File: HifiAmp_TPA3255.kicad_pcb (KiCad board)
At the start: 4 copper layers, 200 x 150 mm, 124 parts, among them J1 PVDD 48V IN — NEEDS_DATA, J2 RCA L SE, J3 RCA R SE, J301 SPK_L, J302 SPK_R, J4 VOLUME_REMOTE, Q301 IPP330P10NM, Q302 IXTK200N10L2, U1 LM5010ASD, U2 LM2940IMP-12/NOPB, U3 TLV1117-33IDCY, U4 OPA1612AIDR, U5 OPA1612AIDR, U6 TPA3255B, U7 TPS3802K33DCKR, U8 LM5069-2

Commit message: feat(f1.1): route the auxiliary rails, and prove VBG cannot cross
AVDD, DVDD and +12V now reach their decoupling capacitors: 15 segments on
F.Cu, no via, 0.30 mm wide. The class width of 0.8 mm was never an option at
U6's 0.635 mm pitch — 0.30 mm leaves 0.285 mm of clearance where 0.25 is
required, and the classes had to be read from .kicad_pro, not the .kicad_dru.

A first attempt shorted six items: C106, C107, C206 and C207 sit in the
corridor and were missing from the obstacle list. The DRC caught what the
script did not. Those 14 segments were pulled and the geometry recomputed.

VBG stays unrouted, and not for lack of trying. At U6 pin 22 comes before
VBG; at the capacitors C303 comes before C304. The order inverts between
source and target, so any single-layer path crosses — the external detour
runs into AVDD, the local bypass needs 0.75 mm where a 0805 offers 0.65, and
yielding priority hits the same neck. No via was placed: that call is the
user's.

DRC unchanged at 112 silkscreen violations, no clearance, no shorting items,
no dangling track; parity still 3; unconnected 244 to 239, exactly the five
ratsnests predicted.

Co-Authored-By: Claude Opus 5 <noreply@anthropic.com>
Claude-Session: https://claude.ai/code/session_01Q198zQg99VJYE128nree8X
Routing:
- net /DVDD: track 0.00 -> 38.3 mm
- net /AVDD: track 0.00 -> 32.4 mm
- net /+12V: track 0.00 -> 17.3 mm
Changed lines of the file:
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@@
 		(tags "capacitor")
 		(property "Reference" "C310"
-			(at 0 -2.3 -90)
+			(at 0 -2.3 270)
 			(layer "F.SilkS")
 			(effects
@@
 		)
 		(property "Value" "1uF/100V"
-			(at 0 2.3 -90)
+			(at 0 2.3 270)
 			(layer "F.Fab")
 			(effects
@@
 		)
 		(property "Datasheet" ""
-			(at 0 0 -90)
+			(at 0 0 270)
 			(layer "F.Fab")
 			(hide yes)
@@
 		)
 		(property "Description" ""
-			(at 0 0 -90)
+			(at 0 0 270)
 			(layer "F.Fab")
 			(hide yes)
@@
 		)
 		(property "KiLib_Generator" "SMD_2terminal_chip_molded"
-			(at 0 0 -90)
+			(at 0 0 270)
 			(layer "F.SilkS")
 			(hide yes)
@@
 		)
 		(fp_text user "${REFERENCE}"
-			(at 0 0 -90)
+			(at 0 0 270)
 			(layer "F.Fab")
 			(effects
@@
 	)
 	(segment
+		(start 288.7125 181.6675)
+		(end 288.7125 185.5)
+		(width 0.3)
+		(layer "F.Cu")
+		(net "/+12V")
+	)
+	(segment
+		(start 292.225 165)
+		(end 292.225 166)
+		(width 0.3)
+		(layer "F.Cu")
+		(net "/+12V")
+	)
+	(segment
+		(start 292.225 185.5)
+		(end 292.225 184)
+		(width 0.3)
+		(layer "F.Cu")
+		(net "/+12V")
+	)
+	(segment
+		(start 288.7125 168.3325)
+		(end 288.7125 165)
+		(width 0.3)
+		(layer "F.Cu")
+		(net "/+12V")
+	)
+	(segment
+		(start 288.7125 165)
+		(end 292.225 165)
+		(width 0.3)
+		(layer "F.Cu")
+		(net "/+12V")
+	)
+	(segment
+		(start 288.7125 185.5)
+		(end 292.225 185.5)
+		(width 0.3)
+		(layer "F.Cu")
+		(net "/+12V")
+	)
+	(segment
+		(start 288.7125 181.0325)
+		(end 288.7125 181.6675)
+		(width 0.3)
+		(layer "F.Cu")
+		(net "/+12V")
+	)
+	(segment
 		(start 279.9 177.2225)
 		(end 281.2875 177.2225)
@@
 	)
 	(segment
+		(start 298.7 195)
+		(end 292.05 195)
+		(width 0.3)
+		(layer "F.Cu")
+		(net "/DVDD")
+	)
+	(segment
+		(start 288.7125 175.3175)
+		(end 298.7 175.3175)
+		(width 0.3)
+		(layer "F.Cu")
+		(net "/DVDD")
+	)
+	(segment
+		(start 298.7 175.3175)
+		(end 298.7 195)
+		(width 0.3)
+		(layer "F.Cu")
+		(net "/DVDD")
+	)
+	(segment
+		(start 292.05 195)
+		(end 292.05 193)
+		(width 0.3)
+		(layer "F.Cu")
+		(net "/DVDD")
+	)
+	(segment
+		(start 298.7 158.8)
+		(end 292.05 158.8)
+		(width 0.3)
+		(layer "F.Cu")
+		(net "/AVDD")
+	)
+	(segment
+		(start 292.05 158.8)
+		(end 292.05 160)
+		(width 0.3)
+		(layer "F.Cu")
+		(net "/AVDD")
+	)
+	(segment
+		(start 288.7125 173.4125)
+		(end 298.7 173.4125)
+		(width 0.3)
+		(layer "F.Cu")
+		(net "/AVDD")
+	)
+	(segment
+		(start 298.7 173.4125)
+		(end 298.7 158.8)
+		(width 0.3)
+		(layer "F.Cu")
+		(net "/AVDD")
+	)
+	(segment

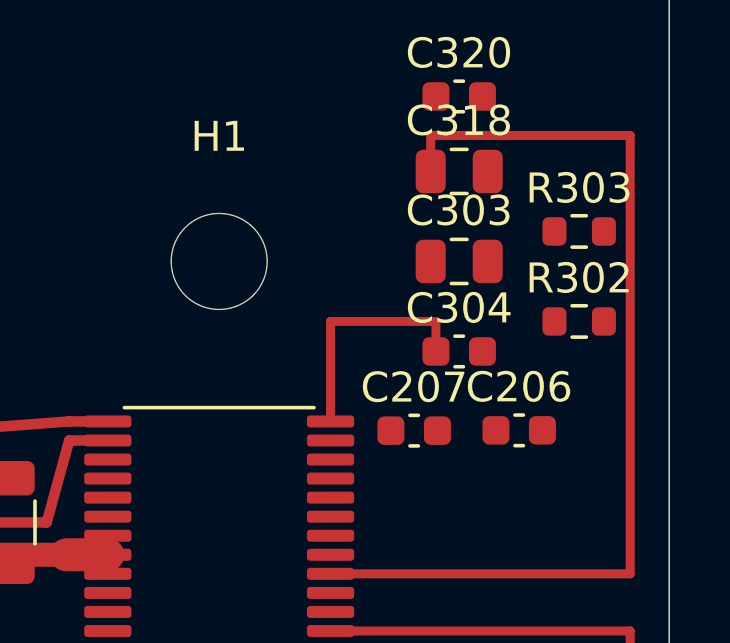
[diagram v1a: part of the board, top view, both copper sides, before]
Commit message: feat(f1.1): swap C303 and C304 so VBG no longer has to cross
The crossing came from the order of the endpoints inverting between U6 and
the capacitor row, so the endpoints are what moved: C303 takes y=166 and
C304 takes y=163. The order now matches on both sides and VBG reaches its
capacitor in a straight run — 4 segments, 14.0 mm at 0.25 mm — with +12V
pin 22 following in 3 segments. Still no via anywhere on the board.

Moving an 0805 into an 0603 row is fine here: both sit at 0 degrees, so the
long axis runs in x and the row only grows 0.5 mm in y. The real obstacle
was never the neighbouring part but the GND pads of C207 and C303, which a
first route came within -0.125 mm of. The clearance check caught it before
the DRC did.

The IPC move left three obsolete /+12V segments dangling behind it. Query a
net's traces after moving one of its components.

Unconnected 239 to 238, parity still 3, no clearance, shorting or dangling
items, 124 footprints with exactly two (at) lines swapped. Silkscreen went
112 to 113 as C303 now overlaps the reference fields of C206 and C207 —
cosmetic, and it joins the pile to be cleared in one pass.

F1.1 is closed.

Co-Authored-By: Claude Opus 5 <noreply@anthropic.com>
Claude-Session: https://claude.ai/code/session_01Q198zQg99VJYE128nree8X
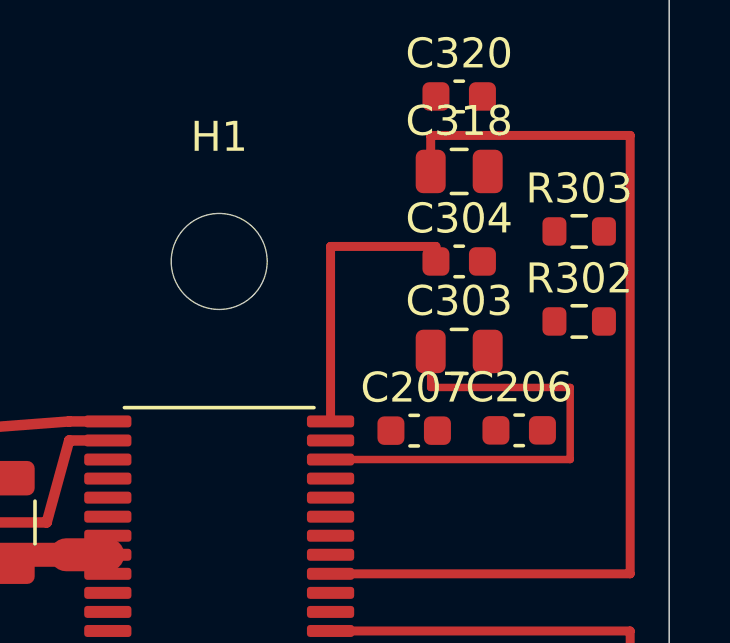
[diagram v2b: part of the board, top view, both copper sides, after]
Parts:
- moved C303 3.00 mm to (293.0, 166.0)
- moved C304 3.00 mm to (293.0, 163.0)
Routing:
- net /VBG: track 0.00 -> 16.2 mm
- net /+12V: track 17.3 -> 19.3 mm
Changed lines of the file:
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@@
 	(footprint "Capacitor_SMD:C_0805_2012Metric"
 		(layer "F.Cu")
-		(at 293 163)
+		(at 293 166)
 		(descr "Capacitor SMD 0805 (2012 Metric), square (rectangular) end terminal, IPC-7351 nominal, (Body size source: IPC-SM-782 page 76, https://www.pcb-3d.com/wordpress/wp-content/uploads/ipc-sm-782a_amendment_1_and_2.pdf, https://docs.google.com/spreadsheets/d/1BsfQQcO9C6DZCsRaXUlFlo91Tg2WpOkGARC1WS5S8t0/edit?usp=sharing)")
 		(tags "capacitor")
@@
 		(sheetname "/")
 		(sheetfile "HifiAmp_TPA3255.kicad_sch")
-		(units
-			(unit
-				(name "A")
-				(pins "1" "2")
-			)
-		)
 		(attr smd)
 		(duplicate_pad_numbers_are_jumpers no)
@@
 	(footprint "Capacitor_SMD:C_0603_1608Metric"
 		(layer "F.Cu")
-		(at 293 166)
+		(at 293 163)
 		(descr "Capacitor SMD 0603 (1608 Metric), square (rectangular) end terminal, IPC-7351 nominal, (Body size source: IPC-SM-782 page 76, https://www.pcb-3d.com/wordpress/wp-content/uploads/ipc-sm-782a_amendment_1_and_2.pdf)")
 		(tags "capacitor")
@@
 		(sheetname "/")
 		(sheetfile "HifiAmp_TPA3255.kicad_sch")
-		(units
-			(unit
-				(name "A")
-				(pins "1" "2")
-			)
-		)
 		(attr smd)
 		(duplicate_pad_numbers_are_jumpers no)
@@
 	)
 	(segment
-		(start 292.225 165)
-		(end 292.225 166)
+		(start 288.7125 168.3325)
+		(end 288.7125 162.5)
 		(width 0.3)
 		(layer "F.Cu")
@@
 	)
 	(segment
-		(start 292.225 185.5)
-		(end 292.225 184)
+		(start 292.225 162.5)
+		(end 292.225 163)
 		(width 0.3)
 		(layer "F.Cu")
@@
 	)
 	(segment
-		(start 288.7125 168.3325)
-		(end 288.7125 165)
+		(start 292.225 185.5)
+		(end 292.225 184)
 		(width 0.3)
 		(layer "F.Cu")
@@
 	)
 	(segment
-		(start 288.7125 165)
-		(end 292.225 165)
+		(start 288.7125 162.5)
+		(end 292.225 162.5)
 		(width 0.3)
 		(layer "F.Cu")
@@
 	)
 	(segment
+		(start 288.7125 169.6025)
+		(end 296.7 169.6025)
+		(width 0.25)
+		(layer "F.Cu")
+		(net "/VBG")
+	)
+	(segment
+		(start 292.05 167.2)
+		(end 292.05 166)
+		(width 0.25)
+		(layer "F.Cu")
+		(net "/VBG")
+	)
+	(segment
+		(start 296.7 167.2)
+		(end 292.05 167.2)
+		(width 0.25)
+		(layer "F.Cu")
+		(net "/VBG")
+	)
+	(segment
+		(start 296.7 169.6025)
+		(end 296.7 167.2)
+		(width 0.25)
+		(layer "F.Cu")
+		(net "/VBG")
+	)
+	(segment

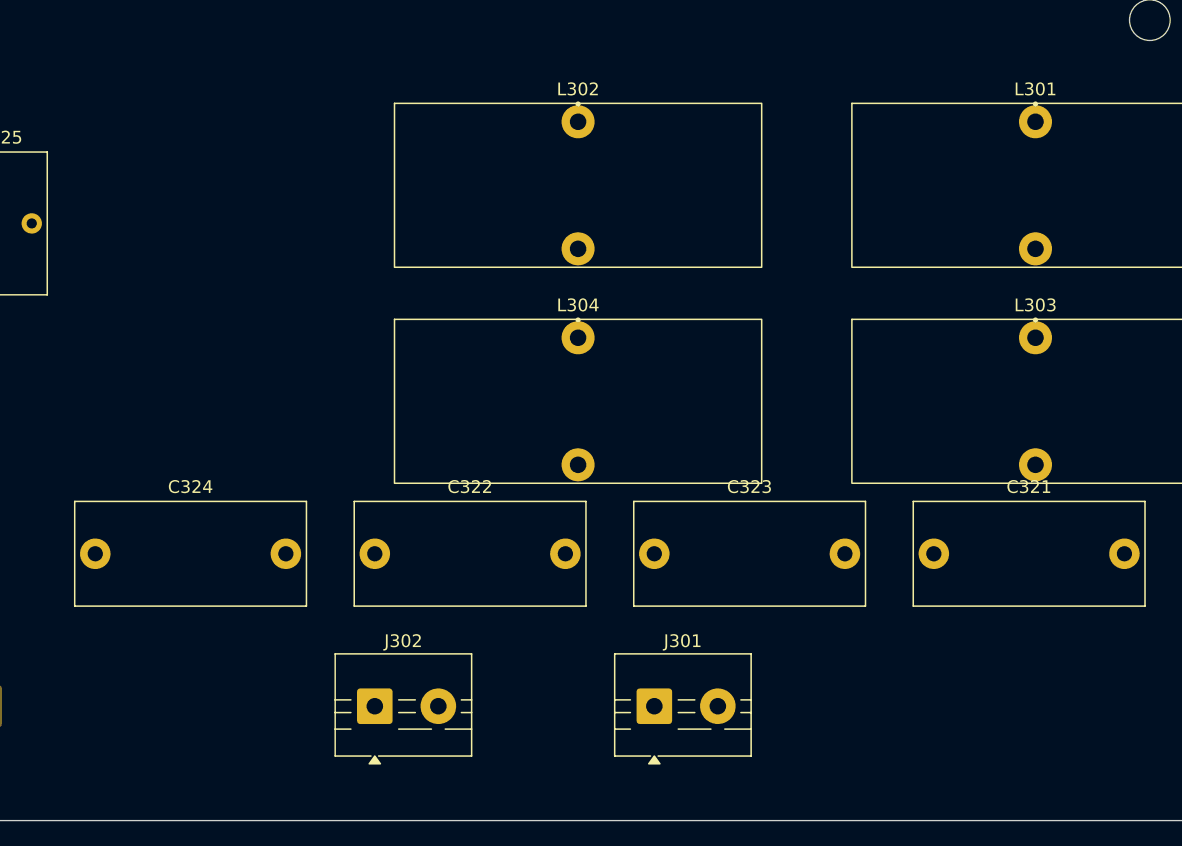
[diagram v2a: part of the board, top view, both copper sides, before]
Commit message: feat(f1.2-a): untangle the outputs, then route them at their class width
The four filtered outputs could not be routed on F.Cu at all with the E1.5
placement, and the obstacle was an order, not a width. At the filter caps the
x-order was D, B, C, A; at the terminals, fixed by BTL pairing, it is D, C, B,
A. B and C transposed force a crossing on any single-layer path, detours along
the board edge included, since D must itself sweep the band to reach its cap at
x = 202. This is exactly the interleaving E1.5 measured and handed to F1.

The fix moves nothing new: L302 and L303 swap slots, C322 and C323 swap slots,
identical parts into identical positions, rotations untouched. The cap order
becomes D, C, B, A and the topology turns planar. It also groups each bridge
pair into one column -- A and B at x = 276, C and D at x = 240 -- which is what
the F1 pairing constraint asked for and the placement could not give. Every
L-to-R symmetry vector stays exact and the intra-pair ones become exact too.

The 0.5 mm draft this replaces carried 1.45 A at IPC-2221, 35 um, dT = 10 C,
for 5 A to pass. At 3.00 mm the track carries 5.3 A, and the class width proves
tenable here: outside a fine-pitch package the obstacles are spaced through-hole
pads. Tightest corridors, checked by hand then by DRC: 0.70 mm under L302's pad,
0.75 mm above the filter caps, 1.50 mm to the board edge.

Pairing target set on real track lengths and met without meanders: 12.0 mm
within A/B, 10.0 mm within C/D, against 8.5 and 26.4 mm as placed. 12 mm of
3 mm track is 2 mOhm and 10 nH against 15 uH and 31 mOhm of series inductor --
meandering would cost copper and loop area for nothing measurable.

DRC 113 violations, the same silkscreen ones as the baseline; no clearance, no
shorting_items, no track_dangling, no solder_mask_bridge, no edge clearance.
Unconnected 238 to 230, the eight predicted ratsnests. Parity still 3. Checked
independently: 58 segments all on F.Cu, 0 vias, zero intersection between the
23 ne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
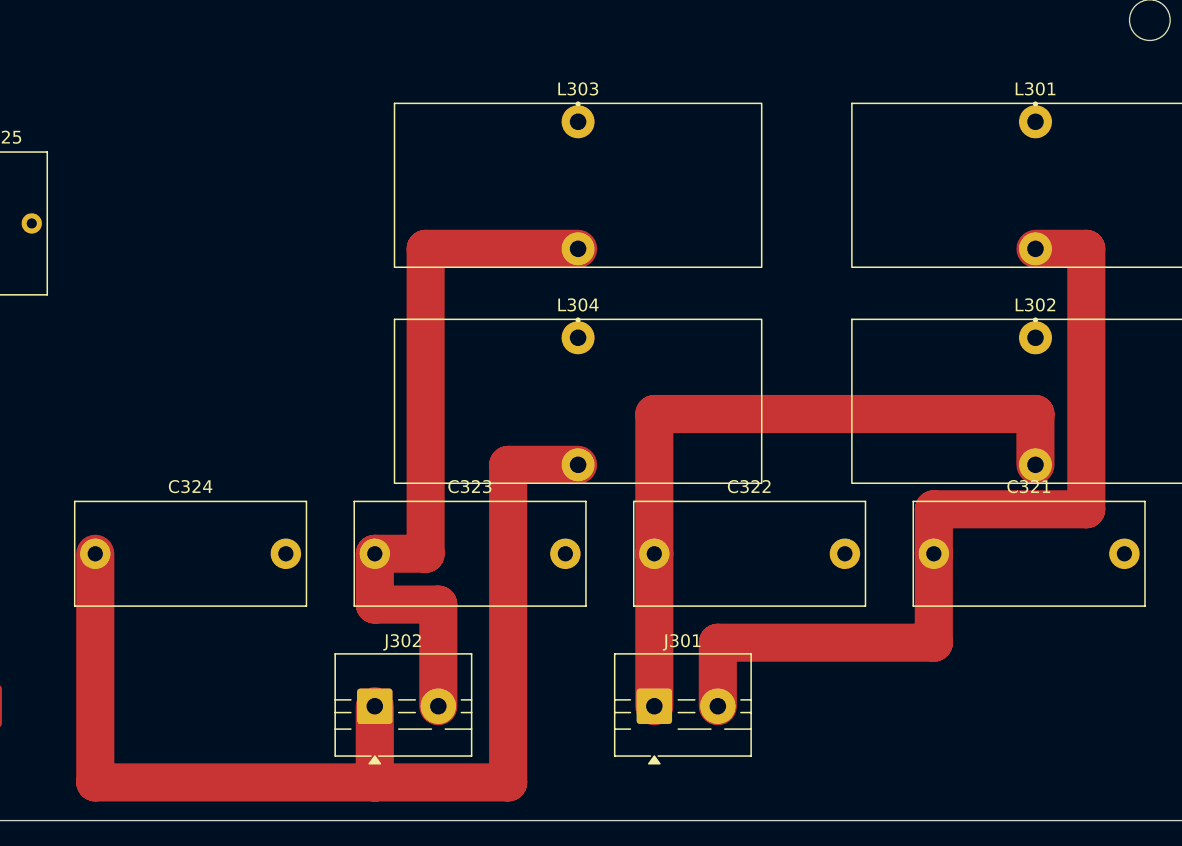
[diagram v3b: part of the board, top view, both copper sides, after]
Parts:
- moved L302 39.8 mm to (276.0, 212.0)
- moved L303 39.8 mm to (240.0, 195.0)
- moved C322 22.0 mm to (246.0, 229.0)
- moved C323 22.0 mm to (224.0, 229.0)
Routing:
- net /OUT_D_F: track 0.00 -> 87.0 mm
- net /OUT_A_F: track 0.00 -> 69.0 mm
- net /OUT_C_F: track 0.00 -> 57.0 mm
- net /OUT_B_F: track 0.00 -> 57.0 mm
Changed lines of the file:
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@@
 	(footprint "Capacitor_THT:C_Rect_L18.0mm_W8.0mm_P15.00mm_FKS3_FKP3"
 		(layer "F.Cu")
-		(at 224 229)
+		(at 246 229)
 		(descr "C, Rect series, Radial, pin pitch=15.00mm, length*width=18*8mm^2, Capacitor, http://www.wima.com/EN/WIMA_FKS_3.pdf")
 		(tags "C Rect series Radial pin pitch 15.00mm length 18mm width 8mm Capacitor")
@@
 	(footprint "Capacitor_THT:C_Rect_L18.0mm_W8.0mm_P15.00mm_FKS3_FKP3"
 		(layer "F.Cu")
-		(at 246 229)
+		(at 224 229)
 		(descr "C, Rect series, Radial, pin pitch=15.00mm, length*width=18*8mm^2, Capacitor, http://www.wima.com/EN/WIMA_FKS_3.pdf")
 		(tags "C Rect series Radial pin pitch 15.00mm length 18mm width 8mm Capacitor")
@@
 	(footprint "HifiAmp_TPA3255_Local:L_Toroid_Vertical_L28.6mm_W12.3mm_P10.00mm_Coilcraft_PA6331"
 		(layer "F.Cu")
-		(at 240 195)
+		(at 276 212)
 		(descr "Coilcraft PA6331-AE, toroidal power inductor 15uH, vertical mount, iron powder core, THT, body 28.6mm max dia x 12.3mm max thickness, pin pitch 10.0+/-0.5mm")
 		(property "Reference" "L302"
@@
 	(footprint "HifiAmp_TPA3255_Local:L_Toroid_Vertical_L28.6mm_W12.3mm_P10.00mm_Coilcraft_PA6331"
 		(layer "F.Cu")
-		(at 276 212)
+		(at 240 195)
 		(descr "Coilcraft PA6331-AE, toroidal power inductor 15uH, vertical mount, iron powder core, THT, body 28.6mm max dia x 12.3mm max thickness, pin pitch 10.0+/-0.5mm")
 		(property "Reference" "L303"
@@
 	)
 	(segment
+		(start 234.5 222)
+		(end 234.5 247)
+		(width 3)
+		(layer "F.Cu")
+		(net "/OUT_D_F")
+	)
+	(segment
+		(start 202 247)
+		(end 202 229)
+		(width 3)
+		(layer "F.Cu")
+		(net "/OUT_D_F")
+	)
+	(segment
+		(start 234.5 247)
+		(end 224 247)
+		(width 3)
+		(layer "F.Cu")
+		(net "/OUT_D_F")
+	)
+	(segment
+		(start 240 222)
+		(end 234.5 222)
+		(width 3)
+		(layer "F.Cu")
+		(net "/OUT_D_F")
+	)
+	(segment
+		(start 224 247)
+		(end 224 241)
+		(width 3)
+		(layer "F.Cu")
+		(net "/OUT_D_F")
+	)
+	(segment
+		(start 224 247)
+		(end 202 247)
+		(width 3)
+		(layer "F.Cu")
+		(net "/OUT_D_F")
+	)
+	(segment
 		(start 298.7 195)
 		(end 292.05 195)
@@
 		(net "/BST_A")
 	)
+	(segment
+		(start 268 236)
+		(end 251 236)
+		(width 3)
+		(layer "F.Cu")
+		(net "/OUT_A_F")
+	)
+	(segment
+		(start 280 205)
+		(end 280 225.5)
+		(width 3)
+		(layer "F.Cu")
+		(net "/OUT_A_F")
+	)
+	(segment
+		(start 268 229)
+		(end 268 236)
+		(width 3)
+		(layer "F.Cu")
+		(net "/OUT_A_F")
+	)
+	(segment
+		(start 276 205)
+		(end 280 205)
+		(width 3)
+		(layer "F.Cu")
+		(net "/OUT_A_F")
+	)
+	(segment
+		(start 268 225.5)
+		(end 268 229)
+		(width 3)
+		(layer "F.Cu")
+		(net "/OUT_A_F")
+	)
+	(segment
+		(start 280 225.5)
+		(end 268 225.5)
+		(width 3)
+		(layer "F.Cu")
+		(net "/OUT_A_F")
+	)
+	(segment
+		(start 251 236)
+		(end 251 241)
+		(width 3)
+		(layer "F.Cu")
+		(net "/OUT_A_F")
+	)
+	(segment
+		(start 246 229)
+		(end 246 241)
+		(width 3)
+		(layer "F.Cu")
+		(net "/OUT_B_F")
+	)
+	(segment
+		(start 246 218)
+		(end 246 229)
+		(width 3)
+		(layer "F.Cu")
+		(net "/OUT_B_F")
+	)
+	(segment
+		(start 276 222)
+		(end 276 218)
+		(width 3)
+		(layer "F.Cu")
+		(net "/OUT_B_F")
+	)
+	(segment
+		(start 276 218)
+		(end 246 218)
+		(width 3)
+		(layer "F.Cu")
+		(net "/OUT_B_F")
+	)
+	(segment
+		(start 228 229)
+		(end 224 229)
+		(width 3)
+		(layer "F.Cu")
+		(net "/OUT_C_F")
+	)
+	(segment
+		(start 224 229)
+		(end 224 233)
+		(width 3)
+		(layer "F.Cu")
+		(net "/OUT_C_F")
+	)
+	(segment
+		(start 224 233)
+		(end 229 233)
+		(width 3)
+		(layer "F.Cu")
+		(net "/OUT_C_F")
+	)
+	(segment
+		(start 240 205)
+		(end 228 205)
+		(width 3)
+		(layer "F.Cu")
+		(net "/OUT_C_F")
+	)
+	(segment
+		(start 229 233)
+		(end 229 241)
+		(width 3)
+		(layer "F.Cu")
+		(net "/OUT_C_F")
+	)
+	(segment
+		(start 228 205)
+		(end 228 229)
+		(width 3)
+		(layer "F.Cu")
+		(net "/OUT_C_F")
+	)
 	(embedded_fonts no)
